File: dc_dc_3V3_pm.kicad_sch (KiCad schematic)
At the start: 15 parts, among them U15 TPS56339DDC

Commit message: fixed i2c3_sda pin (from PA9 to PC9), excluding manual asm components from bom
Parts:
- JP5: now left out of the parts list
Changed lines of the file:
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@@
   )
   (symbol (lib_id "Jumper:Jumper_3_Open") (at 123.825 104.775 90) (unit 1)
-    (in_bom yes) (on_board yes) (dnp no) (fields_autoplaced)
+    (in_bom no) (on_board yes) (dnp no) (fields_autoplaced)
     (property "Reference" "JP5" (at 121.285 103.5049 90)
       (effects (font (size 1.27 1.27)) (justify left))

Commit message: setting 'do not populate' attribute for manually assembled components
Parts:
- JP5: now not fitted; now in the parts list
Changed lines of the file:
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@@
   )
   (symbol (lib_id "Jumper:Jumper_3_Open") (at 123.825 104.775 90) (unit 1)
-    (in_bom no) (on_board yes) (dnp no) (fields_autoplaced)
+    (in_bom yes) (on_board yes) (dnp yes) (fields_autoplaced)
     (property "Reference" "JP5" (at 121.285 103.5049 90)
       (effects (font (size 1.27 1.27)) (justify left))

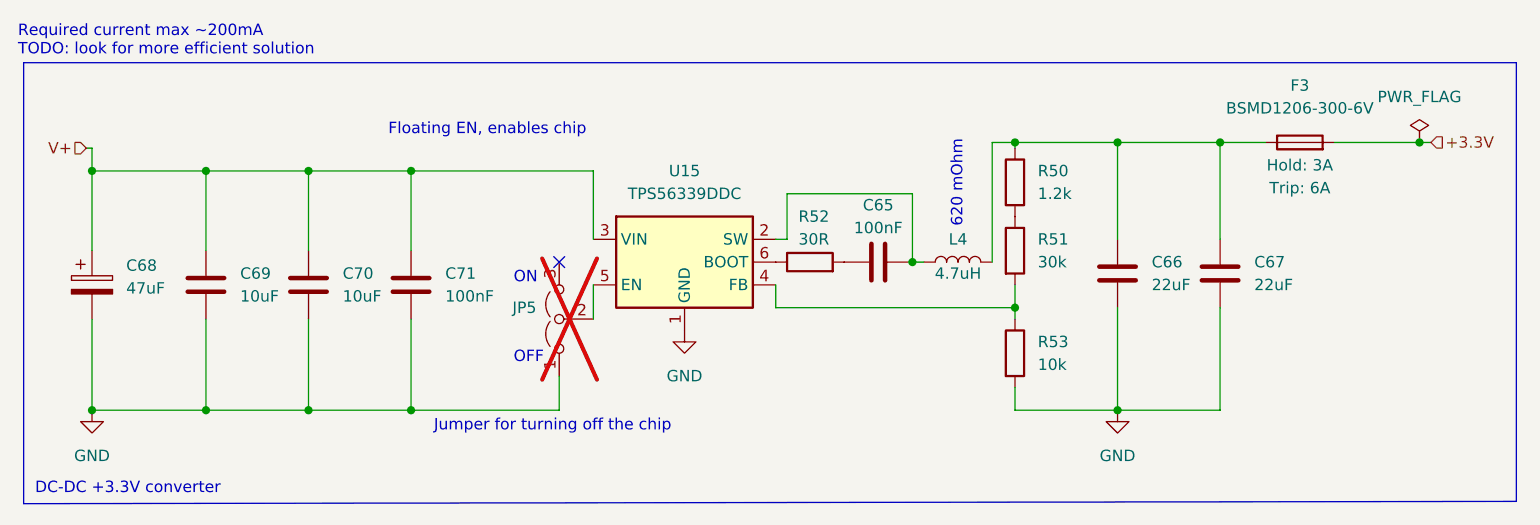
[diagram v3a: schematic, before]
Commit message: updated to kicad 9, added comparator-based power source switching
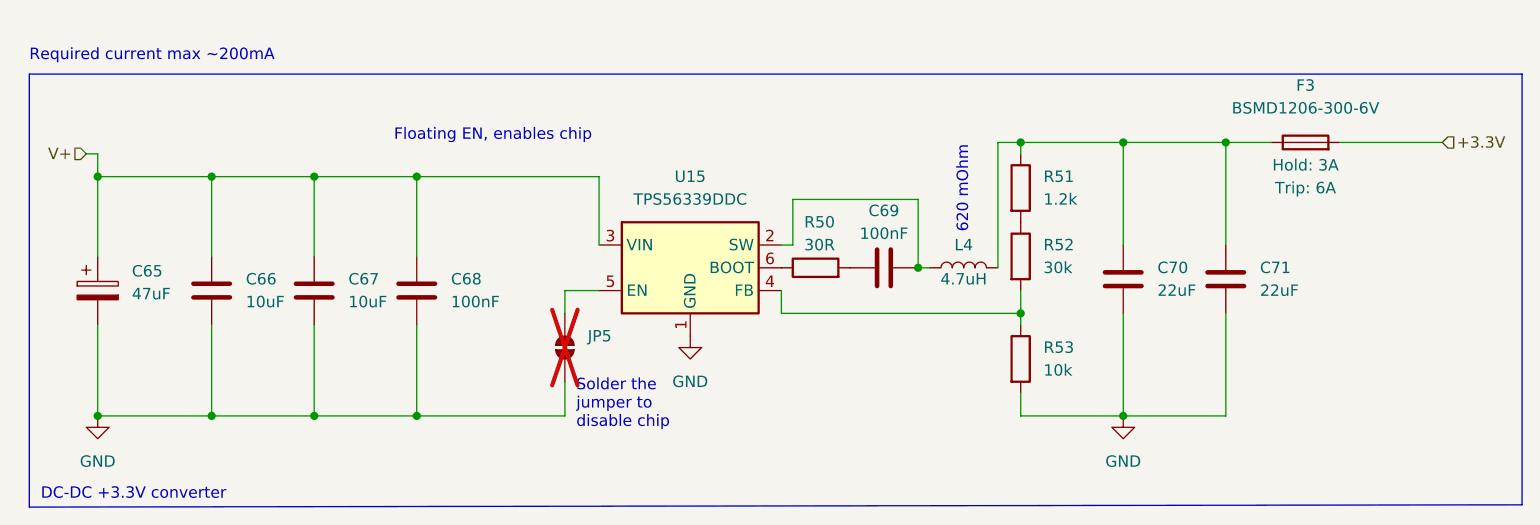
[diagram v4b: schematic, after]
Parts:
- removed JP5: (no value), Connector_PinHeader_2.54mm:PinHeader_1x03_P2.54mm_Vertical, symbol Jumper:Jumper_3_Open
- added JP5: SolderJumper_2_Open, Jumper:SolderJumper-2_P1.3mm_Open_RoundedPad1.0x1.5mm, symbol Jumper:SolderJumper_2_Open
- F3: value BSMD1206-300-6V -> BSMD1206-300-6V
- renumbered C68 to C65, C69 to C66, C70 to C67, C71 to C68, C65 to C69, C66 to C70, C67 to C71, R52 to R50, R50 to R51, R51 to R52
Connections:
- net GND: now also JP5.1 (A)
- net at U15.5 (EN): now also JP5.2 (B)
- no-connect marks 1 -> 0
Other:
- note added: "Required current max ~200mA"
- note added: "Solder the jumper to disable chip"
- note removed: "Jumper for turning off the chip"
- note removed: "OFF"
- note removed: "ON"
- note removed: "Required current max ~200mA TODO: look for more efficient solution"
- moved on the sheet: C65, C66, C67, C68, C69, C70, C71, F3, L4, R50, R51, R52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
